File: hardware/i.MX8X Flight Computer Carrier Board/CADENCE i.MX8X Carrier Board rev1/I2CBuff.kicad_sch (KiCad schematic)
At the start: 0 parts

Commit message: Added pin definitions page
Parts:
- added R102, R103, R108, R109, R110, R111: 330, Resistor_SMD:R_0402_1005Metric, symbol Device:R_US
- added R104, R105, R106, R107, R112, R113, R114, R115: 4.7k, Resistor_SMD:R_0402_1005Metric, symbol Device:R_US
- added U21, U22, U23: P82B715DR, symbol cadence carrier custom symbols:TI_P82B715DR
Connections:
- new net +3.3V: R102.2, R103.2, R104.2, R105.2, R106.2, R107.2, R108.2, R109.2, R110.2, R111.2, R112.2, R113.2, R114.2, R115.2, U21.8 (Vcc), U22.8 (Vcc), U23.8 (Vcc)
- new net GND: U21.4 (GND), U22.4 (GND), U23.4 (GND)
- new net HS_I2C0_SCL: R105.1
- new net HS_I2C0_SDA: R104.1
- new net HS_I2C1_LCL: R110.1, U22.7 (Ly)
- new net HS_I2C1_LDA: R108.1, U22.2 (Lx)
- new net HS_I2C1_SCL: R114.1, U22.6 (Sy)
- new net HS_I2C1_SDA: R112.1, U22.3 (Sx)
- new net HS_I2C2_LCL: R103.1, U21.7 (Ly)
- new net HS_I2C2_LDA: R102.1, U21.2 (Lx)
- new net HS_I2C2_SCL: R107.1, U21.6 (Sy)
- new net HS_I2C2_SDA: R106.1, U21.3 (Sx)
- new net HS_I2C3_LCL: R111.1, U23.7 (Ly)
- new net HS_I2C3_LDA: R109.1, U23.2 (Lx)
- new net HS_I2C3_SCL: R115.1, U23.6 (Sy)
- new net HS_I2C3_SDA: R113.1, U23.3 (Sx)

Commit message: oops the real push here
previous push description/title describes this content push
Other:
- note added: "I2C is unbuffered (onboard connections only)"
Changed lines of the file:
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@@
 	(generator_version "9.0")
 	(paper "A5")
+	(text "I2C is unbuffered (onboard connections only)"
+		(exclude_from_sim no)
+		(at 55.88 22.606 0)
+		(effects
+			(font
+				(size 1.27 1.27)
+				(thickness 0.254)
+				(bold yes)
+			)
+		)
+	)
 	(junction
 		(at 57.15 69.85)

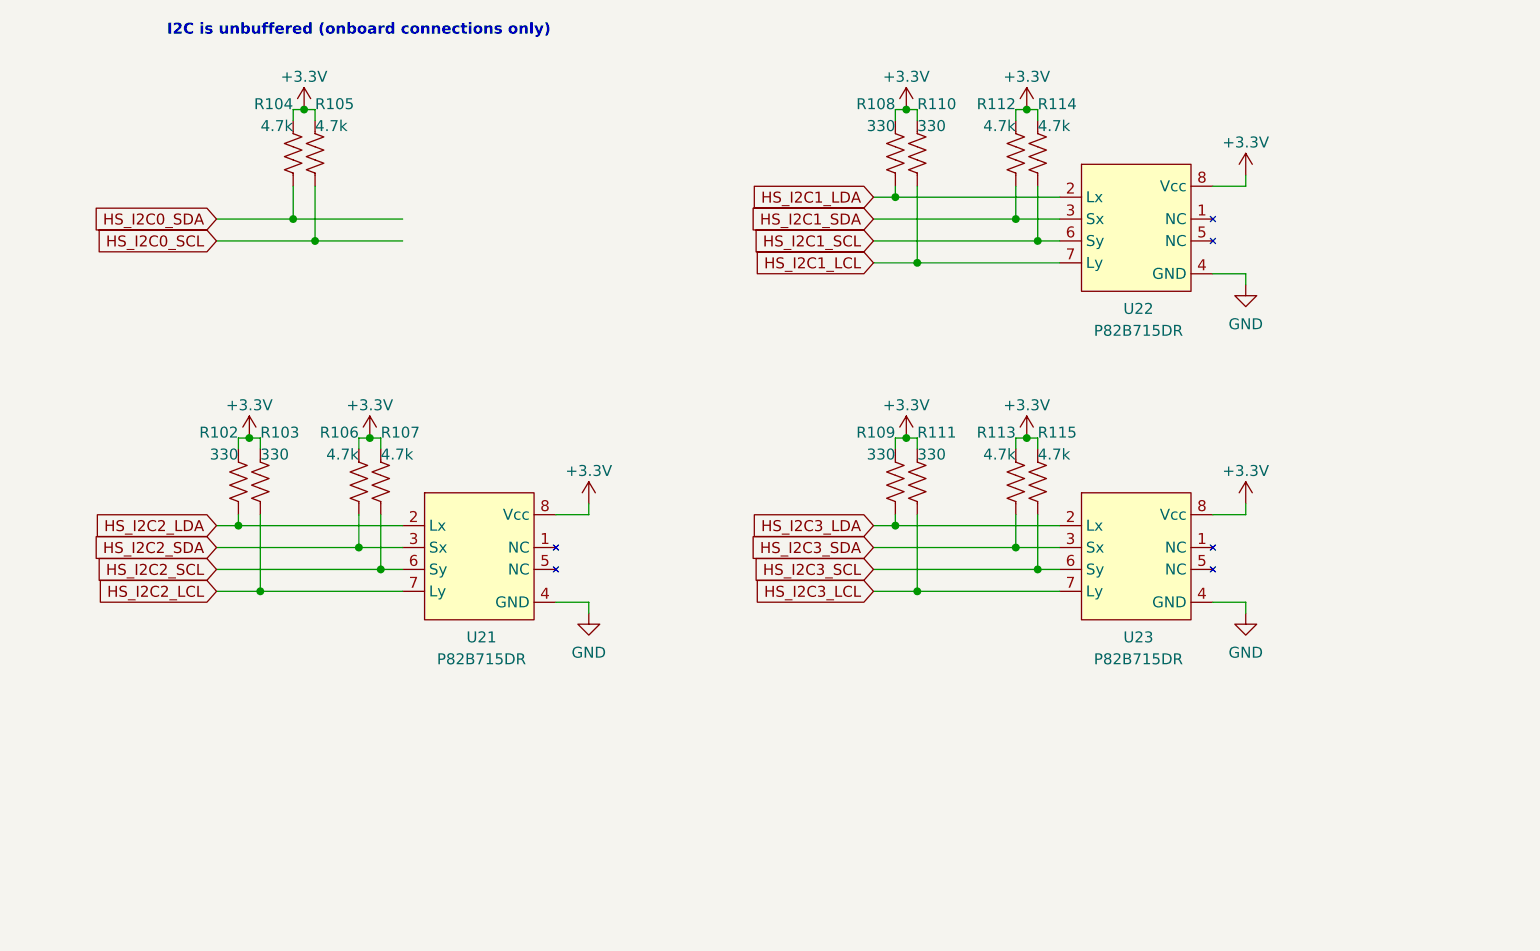
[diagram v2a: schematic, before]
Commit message: Edited a lot based on IMX8x pin muxing tool
- validated watchdog pin
- edited some i2c definitions
- finally updated peripheral connections
- realized that UART0 needed to be reserved for programming flash directly, so routed it to FTDI and added a MUX to have a user selectable UART0 between FTDI and pin header
- shifted around UART 1, 2, and 3 as a result of above realization
- added gpio and level shifters for payload
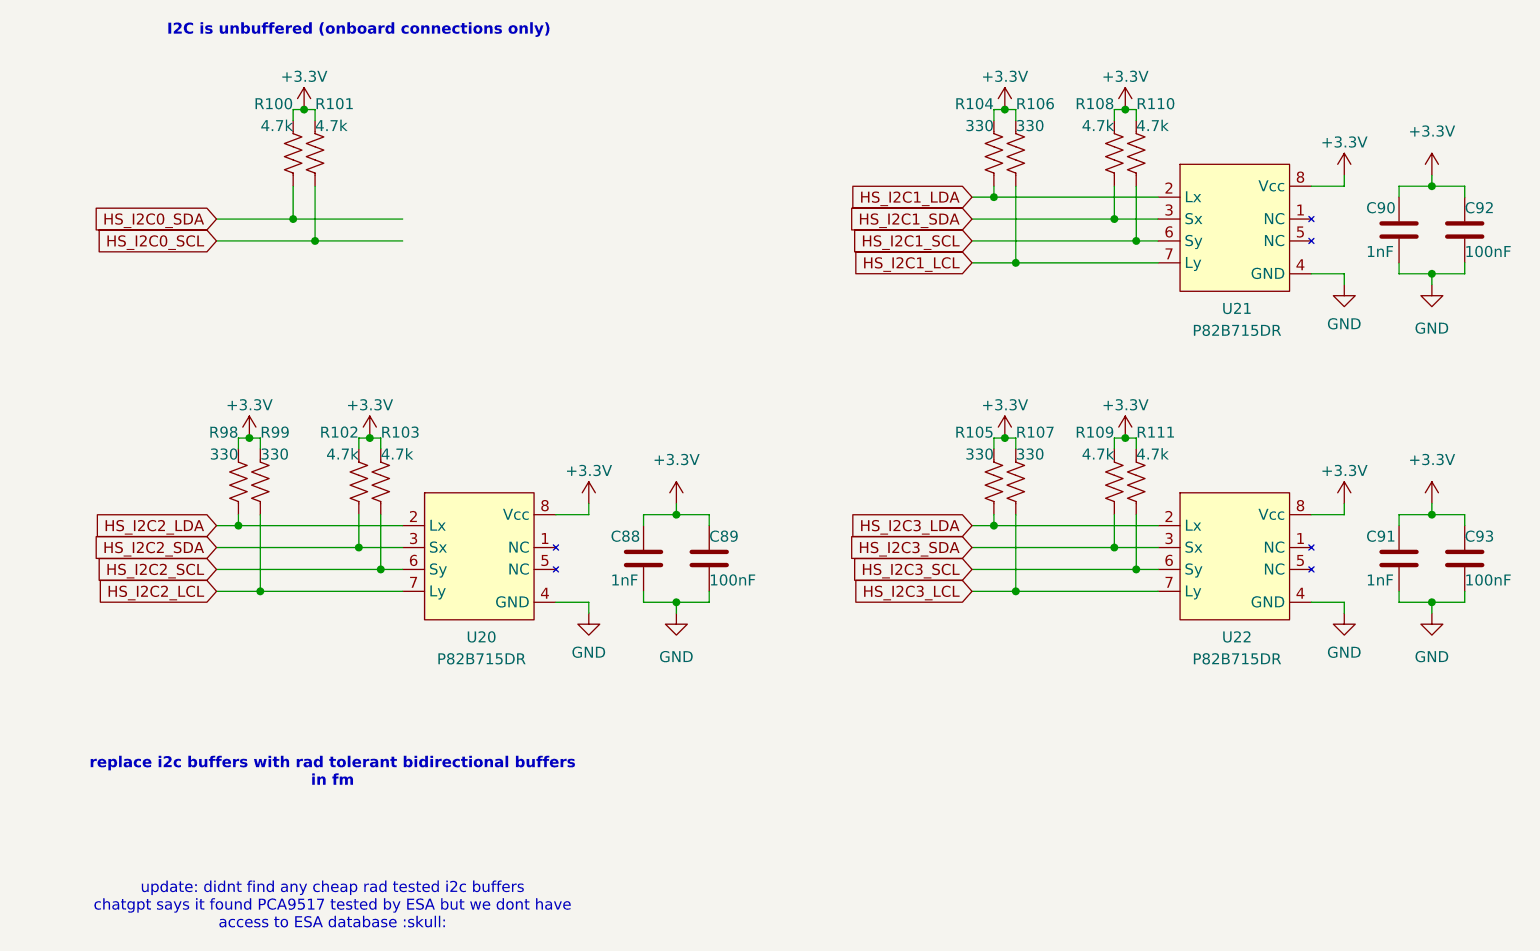
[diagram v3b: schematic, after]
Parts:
- added C88, C90, C91: 1nF, symbol Device:C
- added C89, C92, C93: 100nF, symbol Device:C
- renumbered R104 to R100, R105 to R101, R106 to R102, R107 to R103, R108 to R104, R109 to R105, R110 to R106, R111 to R107, R112 to R108, R113 to R109, R114 to R110, R115 to R111, R102 to R98, R103 to R99, U21 to U20, U22 to U21, U23 to U22
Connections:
- net +3.3V: now also C88.1, C89.1, C90.1, C91.1, C92.1, C93.1
- net GND: now also C88.2, C89.2, C90.2, C91.2, C92.2, C93.2
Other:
- note added: "replace i2c buffers with rad tolerant bidirectional buffers in fm"
- note added: "update: didnt find any cheap rad tested i2c buffers chatgpt says it found PCA9517 tested by ESA but we dont have access to ESA database :skull:"
- moved on the sheet: R104, R105, R106, R107, R108, R109, R110, R111, U21, U22

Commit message: final rev1 schematic changes for phytec
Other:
- note added: "I2C0 is unbuffered (onboard connections only)"
- note removed: "I2C is unbuffered (onboard connections only)"
- note removed: "update: didnt find any cheap rad tested i2c buffers chatgpt says it found PCA9517 tested by ESA but we dont have access to ESA database :skull:"
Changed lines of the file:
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@@
 	(generator_version "9.0")
 	(paper "A5")
-	(text "I2C is unbuffered (onboard connections only)"
+	(text "I2C0 is unbuffered (onboard connections only)"
 		(exclude_from_sim no)
 		(at 55.88 22.606 0)
@@
 		)
 	)
-	(text "update: didnt find any cheap rad tested i2c buffers\nchatgpt says it found PCA9517 tested by ESA but we dont have\naccess to ESA database :skull:"
-		(exclude_from_sim no)
-		(at 52.832 124.206 0)
-		(effects
-			(font
-				(size 1.27 1.27)
-			)
-		)
-	)
 	(text "replace i2c buffers with rad tolerant bidirectional buffers\nin fm"
 		(exclude_from_sim no)
@@
 		(dnp no)
 		(fields_autoplaced yes)
-		(property "Reference" "#PWR0125"
+		(property "Reference" "#PWR0127"
 			(at 92.71 96.52 0)
 			(effects
@@
 			(project "CADENCE i.MX8X Carrier Board rev1"
 				(path "/de284495-d382-47cb-b528-76e440980d40/c9abda44-b435-415f-87cb-f95498594e84"
-					(reference "#PWR0125")
+					(reference "#PWR0127")
 					(unit 1)
 				)
@@
 		(on_board yes)
 		(dnp no)
-		(property "Reference" "#PWR0119"
+		(property "Reference" "#PWR0121"
 			(at 43.18 73.66 0)
 			(effects
@@
 			(project "CADENCE i.MX8X Carrier Board rev1"
 				(path "/de284495-d382-47cb-b528-76e440980d40/c9abda44-b435-415f-87cb-f95498594e84"
-					(reference "#PWR0119")
+					(reference "#PWR0121")
 					(unit 1)
 				)
@@
 		(on_board yes)
 		(dnp no)
-		(property "Reference" "#PWR0123"
+		(property "Reference" "#PWR0125"
 			(at 82.55 96.52 0)
 			(effects
@@
 			(project "CADENCE i.MX8X Carrier Board rev1"
 				(path "/de284495-d382-47cb-b528-76e440980d40/c9abda44-b435-415f-87cb-f95498594e84"
-					(reference "#PWR0123")
+					(reference "#PWR0125")
 					(unit 1)
 				)
@@
 		(on_board yes)
 		(dnp no)
-		(property "Reference" "#PWR0121"
+		(property "Reference" "#PWR0123"
 			(at 57.15 73.66 0)
 			(effects
@@
 			(project "CADENCE i.MX8X Carrier Board rev1"
 				(path "/de284495-d382-47cb-b528-76e440980d40/c9abda44-b435-415f-87cb-f95498594e84"
-					(reference "#PWR0121")
+					(reference "#PWR0123")
 					(unit 1)
 				)
@@
 		(on_board yes)
 		(dnp no)
-		(property "Reference" "#PWR0131"
+		(property "Reference" "#PWR0133"
 			(at 170.18 58.42 0)
 			(effects
@@
 			(project "CADENCE i.MX8X Carrier Board rev1"
 				(path "/de284495-d382-47cb-b528-76e440980d40/c9abda44-b435-415f-87cb-f95498594e84"
-					(reference "#PWR0131")
+					(reference "#PWR0133")
 					(unit 1)
 				)
@@
 		(dnp no)
 		(fields_autoplaced yes)
-		(property "Reference" "#PWR0135"
+		(property "Reference" "#PWR0137"
 			(at 180.34 58.42 0)
 			(effects
@@
 			(project "CADENCE i.MX8X Carrier Board rev1"
 				(path "/de284495-d382-47cb-b528-76e440980d40/c9abda44-b435-415f-87cb-f95498594e84"
-					(reference "#PWR0135")
+					(reference "#PWR0137")
 					(unit 1)
 				)
@@
 		(on_board yes)
 		(dnp no)
-		(property "Reference" "#PWR0132"
+		(property "Reference" "#PWR0134"
 			(at 170.18 81.28 0)
 			(effects
@@
 			(project "CADENCE i.MX8X Carrier Board rev1"
 				(path "/de284495-d382-47cb-b528-76e440980d40/c9abda44-b435-415f-87cb-f95498594e84"
-					(reference "#PWR0132")
+					(reference "#PWR0134")
 					(unit 1)
 				)
@@
 		(dnp no)
 		(fields_autoplaced yes)
-		(property "Reference" "#PWR0124"
+		(property "Reference" "#PWR0126"
 			(at 92.71 81.28 0)
 			(effects
@@
 			(project "CADENCE i.MX8X Carrier Board rev1"
 				(path "/de284495-d382-47cb-b528-76e440980d40/c9abda44-b435-415f-87cb-f95498594e84"
-					(reference "#PWR0124")
+					(reference "#PWR0126")
 					(unit 1)
 				)
@@
 		(dnp no)
 		(fields_autoplaced yes)
-		(property "Reference" "#PWR0137"
+		(property "Reference" "#PWR0139"
 			(at 180.34 96.52 0)
 			(effects
@@
 			(project "CADENCE i.MX8X Carrier Board rev1"
 				(path "/de284495-d382-47cb-b528-76e440980d40/c9abda44-b435-415f-87cb-f95498594e84"
-					(reference "#PWR0137")
+					(reference "#PWR0139")
 					(unit 1)
 				)
@@
 		(on_board yes)
 		(dnp no)
-		(property "Reference" "#PWR0129"
+		(property "Reference" "#PWR0131"
 			(at 144.78 73.66 0)
 			(effects
@@
 			(project "CADENCE i.MX8X Carrier Board rev1"
 				(path "/de284495-d382-47cb-b528-76e440980d40/c9abda44-b435-415f-87cb-f95498594e84"
-					(reference "#PWR0129")
+					(reference "#PWR0131")
 					(unit 1)
 				)
@@
 		(on_board yes)
 		(dnp no)
-		(property "Reference" "#PWR0126"
+		(property "Reference" "#PWR0128"
 			(at 130.81 35.56 0)
 			(effects
@@
 			(project "CADENCE i.MX8X Carrier Board rev1"
 				(path "/de284495-d382-47cb-b528-76e440980d40/c9abda44-b435-415f-87cb-f95498594e84"
-					(reference "#PWR0126")
+					(reference "#PWR0128")
 					(unit 1)
 				)
@@
 		(dnp no)
 		(fields_autoplaced yes)
-		(property "Reference" "#PWR0134"
+		(property "Reference" "#PWR0136"
 			(at 180.34 43.18 0)
 			(effects
@@
 			(project "CADENCE i.MX8X Carrier Board rev1"
 				(path "/de284495-d382-47cb-b528-76e440980d40/c9abda44-b435-415f-87cb-f95498594e84"
-					(reference "#PWR0134")
+					(reference "#PWR0136")
 					(unit 1)
 				)
@@
 		(on_board yes)
 		(dnp no)
-		(property "Reference" "#PWR0133"
+		(property "Reference" "#PWR0135"
 			(at 170.18 96.52 0)
 			(effects
@@
 			(project "CADENCE i.MX8X Carrier Board rev1"
 				(path "/de284495-d382-47cb-b528-76e440980d40/c9abda44-b435-415f-87cb-f95498594e84"
-					(reference "#PWR0133")
+					(reference "#PWR0135")
 					(unit 1)
 				)
@@
 		(dnp no)
 		(fields_autoplaced yes)
-		(property "Reference" "#PWR0136"
+		(property "Reference" "#PWR0138"
 			(at 180.34 81.28 0)
 			(effects
@@
 			(project "CADENCE i.MX8X Carrier Board rev1"
 				(path "/de284495-d382-47cb-b528-76e440980d40/c9abda44-b435-415f-87cb-f95498594e84"
-					(reference "#PWR0136")
+					(reference "#PWR0138")
 					(unit 1)
 				)
@@
 		(on_board yes)
 		(dnp no)
-		(property "Reference" "#PWR0122"
+		(property "Reference" "#PWR0124"
 			(at 82.55 81.28 0)
 			(effects
@@
 			(project "CADENCE i.MX8X Carrier Board rev1"
 				(path "/de284495-d382-47cb-b528-76e440980d40/c9abda44-b435-415f-87cb-f95498594e84"
-					(reference "#PWR0122")
+					(reference "#PWR0124")
 					(unit 1)
 				)
@@
 		(on_board yes)
 		(dnp no)
-		(property "Reference" "#PWR0130"
+		(property "Reference" "#PWR0132"
 			(at 170.18 43.18 0)
 			(effects
@@
 			(project "CADENCE i.MX8X Carrier Board rev1"
 				(path "/de284495-d382-47cb-b528-76e440980d40/c9abda44-b435-415f-87cb-f95498594e84"
-					(reference "#PWR0130")
+					(reference "#PWR0132")
 					(unit 1)
 				)
@@
 		(on_board yes)
 		(dnp no)
-		(property "Reference" "#PWR0128"
+		(property "Reference" "#PWR0130"
 			(at 144.78 35.56 0)
 			(effects
@@
 			(project "CADENCE i.MX8X Carrier Board rev1"
 				(path "/de284495-d382-47cb-b528-76e440980d40/c9abda44-b435-415f-87cb-f95498594e84"
-					(reference "#PWR0128")
+					(reference "#PWR0130")
 					(unit 1)
 				)
@@
 		(on_board yes)
 		(dnp no)
-		(property "Reference" "#PWR0120"
+		(property "Reference" "#PWR0122"
 			(at 49.53 35.56 0)
 			(effects
@@
 			(project "CADENCE i.MX8X Carrier Board rev1"
 				(path "/de284495-d382-47cb-b528-76e440980d40/c9abda44-b435-415f-87cb-f95498594e84"
-					(reference "#PWR0120")
+					(reference "#PWR0122")
 					(unit 1)
 				)
@@
 		(on_board yes)
 		(dnp no)
-		(property "Reference" "#PWR0127"
+		(property "Reference" "#PWR0129"
 			(at 130.81 73.66 0)
 			(effects
@@
 			(project "CADENCE i.MX8X Carrier Board rev1"
 				(path "/de284495-d382-47cb-b528-76e440980d40/c9abda44-b435-415f-87cb-f95498594e84"
-					(reference "#PWR0127")
+					(reference "#PWR0129")
 					(unit 1)
 				)

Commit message: updated imx8x footprints
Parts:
- C92, C93: footprint (none) -> Capacitor_SMD:C_0603_1608Metric
- U20, U21, U22: footprint (none) -> Footprints:SOIC127P600X175-8N
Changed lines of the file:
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@@
 			)
 		)
-		(property "Footprint" ""
+		(property "Footprint" "Capacitor_SMD:C_0603_1608Metric"
 			(at 185.1152 49.53 0)
 			(effects
@@
 			)
 		)
-		(property "Footprint" ""
+		(property "Footprint" "Footprints:SOIC127P600X175-8N"
 			(at 69.85 76.2 0)
 			(effects
@@
 			)
 		)
-		(property "Footprint" ""
+		(property "Footprint" "Capacitor_SMD:C_0603_1608Metric"
 			(at 185.1152 87.63 0)
 			(effects
@@
 			)
 		)
-		(property "Footprint" ""
+		(property "Footprint" "Footprints:SOIC127P600X175-8N"
 			(at 157.48 38.1 0)
 			(effects
@@
 			)
 		)
-		(property "Footprint" ""
+		(property "Footprint" "Footprints:SOIC127P600X175-8N"
 			(at 157.48 76.2 0)
 			(effects

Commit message: added footprints to imx8x, just need to finish usb, capacitors, and inductors
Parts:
- C88, C89, C90, C91: footprint (none) -> Capacitor_SMD:C_0603_1608Metric
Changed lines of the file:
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@@
 			)
 		)
-		(property "Footprint" ""
+		(property "Footprint" "Capacitor_SMD:C_0603_1608Metric"
 			(at 97.4852 87.63 0)
 			(effects
@@
 			)
 		)
-		(property "Footprint" ""
+		(property "Footprint" "Capacitor_SMD:C_0603_1608Metric"
 			(at 177.4952 87.63 0)
 			(effects
@@
 			)
 		)
-		(property "Footprint" ""
+		(property "Footprint" "Capacitor_SMD:C_0603_1608Metric"
 			(at 89.8652 87.63 0)
 			(effects
@@
 			)
 		)
-		(property "Footprint" ""
+		(property "Footprint" "Capacitor_SMD:C_0603_1608Metric"
 			(at 177.4952 49.53 0)
 			(effects
